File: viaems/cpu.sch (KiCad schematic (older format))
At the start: 33 parts, among them J15 Conn_01x04, J16 USB_B_Micro, J17 Conn_ARM_JTAG_SWD_10, U10 MCP2562-H-SN, U11 NCP1117-3.3_TO252, U9 STM32F407VGTx, Y1 8 Mhz

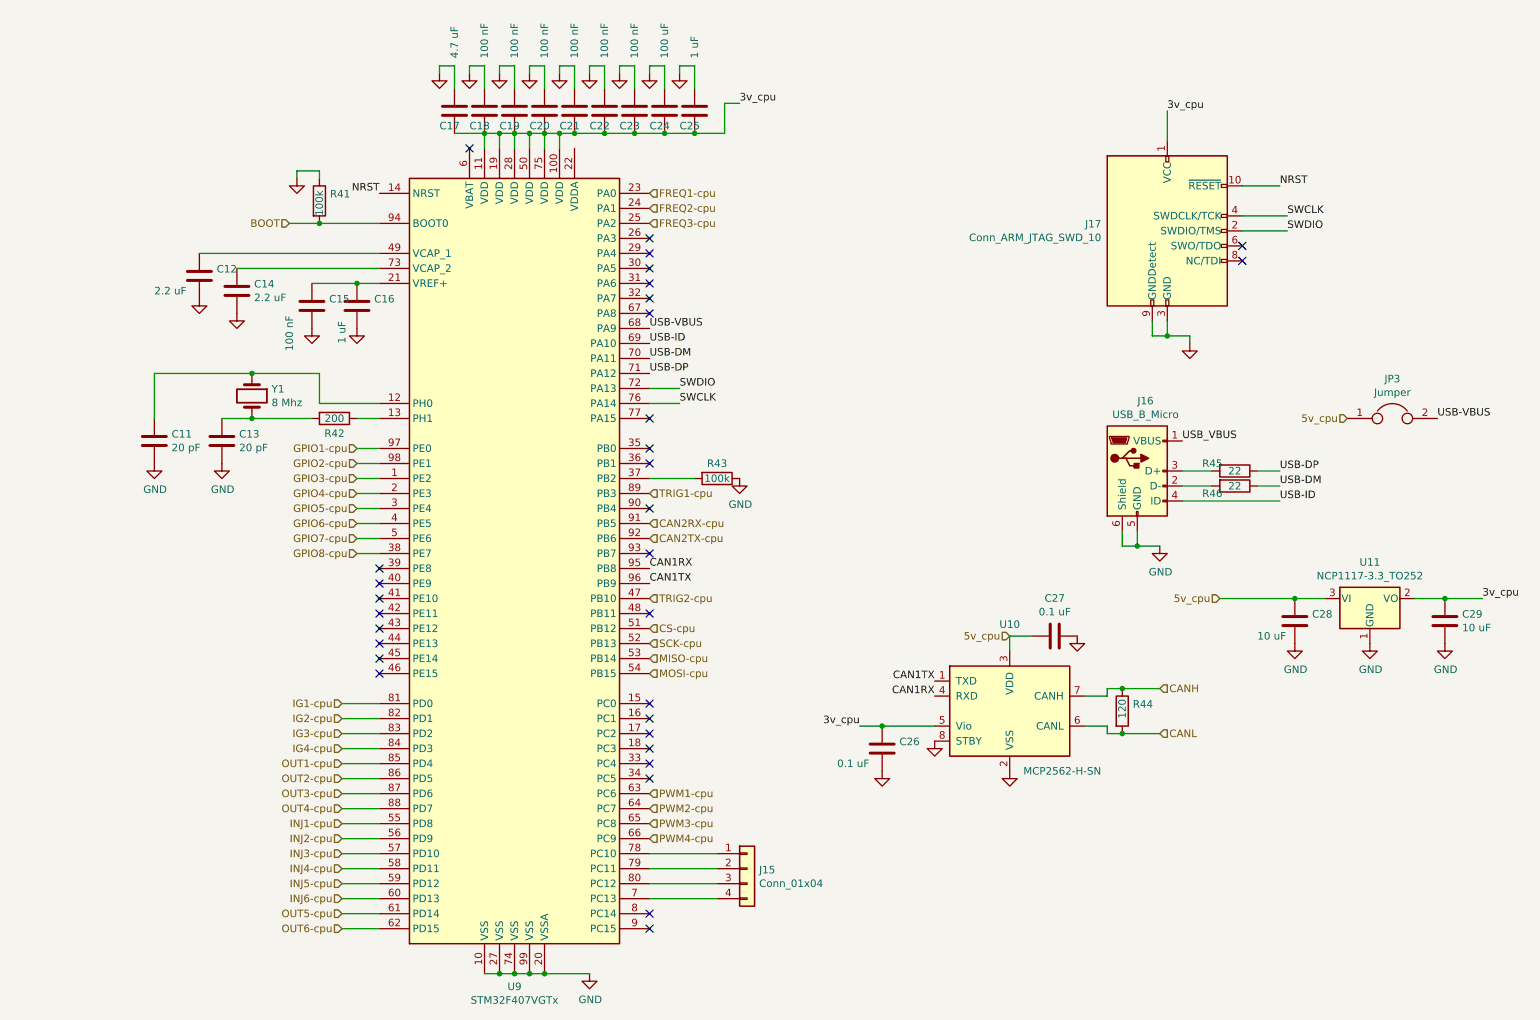
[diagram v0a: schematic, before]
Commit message: More progress. Calling schematic complete, board partially routed
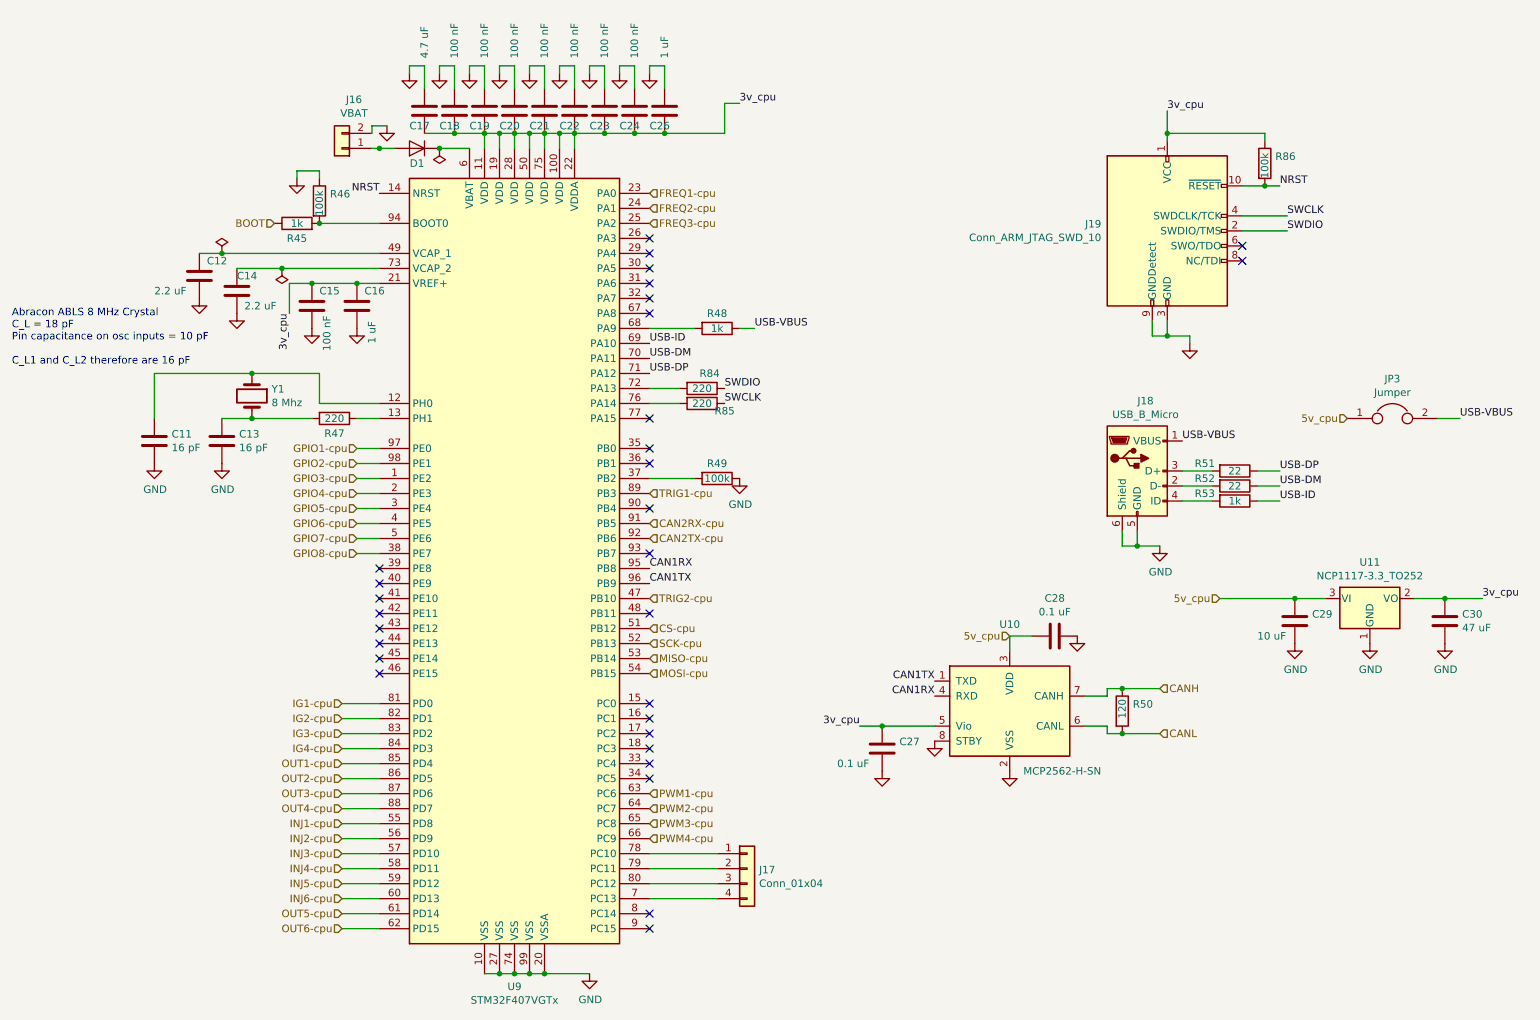
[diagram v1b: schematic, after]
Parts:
- removed C24: 100 uF, symbol Device:C
- added C18: 100 nF, Capacitor_SMD:C_0805_2012Metric_Pad1.15x1.40mm_HandSolder, symbol Device:C
- added D1: D, Diode_SMD:D_0805_2012Metric_Pad1.15x1.40mm_HandSolder, symbol Device:D
- added J16: VBAT, Connector_PinHeader_2.54mm:PinHeader_1x02_P2.54mm_Vertical, symbol Connector_Generic:Conn_01x02
- added R45, R48, R53: 1k, Resistor_SMD:R_0805_2012Metric_Pad1.15x1.40mm_HandSolder, symbol Device:R
- added R84, R85: 220, Resistor_SMD:R_0805_2012Metric_Pad1.15x1.40mm_HandSolder, symbol Device:R
- added R86: 100k, Resistor_SMD:R_0805_2012Metric_Pad1.15x1.40mm_HandSolder, symbol Device:R
- C11, C13: value 20 pF -> 16 pF; footprint (none) -> Capacitor_SMD:C_0805_2012Metric_Pad1.15x1.40mm_HandSolder
- C12, C14, C15, C16, C17: footprint (none) -> Capacitor_SMD:C_0805_2012Metric_Pad1.15x1.40mm_HandSolder
- C19: renamed from C18; footprint (none) -> Capacitor_SMD:C_0805_2012Metric_Pad1.15x1.40mm_HandSolder
- C20: renamed from C19; footprint (none) -> Capacitor_SMD:C_0805_2012Metric_Pad1.15x1.40mm_HandSolder
- C21: renamed from C20; footprint (none) -> Capacitor_SMD:C_0805_2012Metric_Pad1.15x1.40mm_HandSolder
- C22: renamed from C21; footprint (none) -> Capacitor_SMD:C_0805_2012Metric_Pad1.15x1.40mm_HandSolder
- C23: renamed from C22; footprint (none) -> Capacitor_SMD:C_0805_2012Metric_Pad1.15x1.40mm_HandSolder
- C24: renamed from C23; footprint (none) -> Capacitor_SMD:C_0805_2012Metric_Pad1.15x1.40mm_HandSolder
- C26: renamed from C25; footprint (none) -> Capacitor_SMD:C_0805_2012Metric_Pad1.15x1.40mm_HandSolder
- C27: renamed from C26; footprint (none) -> Capacitor_SMD:C_0805_2012Metric_Pad1.15x1.40mm_HandSolder
- C28: renamed from C27; footprint (none) -> Capacitor_SMD:C_0805_2012Metric_Pad1.15x1.40mm_HandSolder
- C29: renamed from C28; footprint (none) -> Capacitor_SMD:C_0805_2012Metric_Pad1.15x1.40mm_HandSolder; Digikey-Part (none) -> 587-3417-1-ND
- C30: renamed from C29; value 10 uF -> 47 uF; footprint (none) -> Capacitor_SMD:C_1206_3216Metric_Pad1.42x1.75mm_HandSolder; Digikey-Part (none) -> 478-9009-1-ND
- J17: renamed from J15; footprint (none) -> Connector_PinHeader_2.54mm:PinHeader_1x04_P2.54mm_Vertical
- J18: renamed from J16; footprint (none) -> Connector_USB:USB_Micro-B_Amphenol_10103594-0001LF_Horizontal; Digikey-Part (none) -> H125279CT-ND
- J19: renamed from J17; Digikey-Part (none) -> SAM9438-ND
- JP3: footprint (none) -> Connector_PinHeader_2.54mm:PinHeader_1x02_P2.54mm_Vertical
- R46: renamed from R41; footprint (none) -> Resistor_SMD:R_0805_2012Metric_Pad1.15x1.40mm_HandSolder
- R47: renamed from R42; value 200 -> 220; footprint (none) -> Resistor_SMD:R_0805_2012Metric_Pad1.15x1.40mm_HandSolder
- R49: renamed from R43; footprint (none) -> Resistor_SMD:R_0805_2012Metric_Pad1.15x1.40mm_HandSolder
- R50: renamed from R44; footprint (none) -> Resistor_SMD:R_0805_2012Metric_Pad1.15x1.40mm_HandSolder
- R51: renamed from R45; footprint (none) -> Resistor_SMD:R_0805_2012Metric_Pad1.15x1.40mm_HandSolder
- R52: renamed from R46; footprint (none) -> Resistor_SMD:R_0805_2012Metric_Pad1.15x1.40mm_HandSolder
- U11: Digikey-Part (none) -> NCP1117DT33T5GOSCT-ND
- Y1: footprint (none) -> Crystal:Crystal_HC49-U_Vertical; Digikey-Part (none) -> 535-10212-1-ND
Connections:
- net USB_VBUS is gone; now on net USB-VBUS: J18.1 (VBUS)
- net 3v_cpu: now also C15.1, C16.1, U9.21 (VREF+), U9.22 (VDDA), C18.2, R86.1
- net BOOT: now also R45.1; no longer R46.2, U9.94 (BOOT0)
- net GND: now also C18.1, J16.2 (Pin_2)
- net NRST: now also R86.2
- net SWCLK: now also R85.1; no longer U9.76 (PA14)
- net SWDIO: now also R84.1; no longer U9.72 (PA13)
- net USB-ID: now also R53.1; no longer J18.4 (ID)
- net USB-VBUS: now also R48.1; no longer U9.68 (PA9)
- net at U9.6 (VBAT): now also D1.1 (K)
- new net: R45.2, R46.2, U9.94 (BOOT0)
- new net: R48.2, U9.68 (PA9)
- new net: R84.2, U9.72 (PA13)
- new net: R85.2, U9.76 (PA14)
- new net: J18.4 (ID), R53.2
- new net: D1.2 (A), J16.1 (Pin_1)
- no-connect marks 31 -> 30
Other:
- note added: "Abracon ABLS 8 MHz Crystal\nC_L = 18 pF\nPin capacitance on osc inputs = 10 pF\n\nC_L1 and C_L2 therefore are 16 pF"
- moved on the sheet: C17, C26

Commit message: More routing
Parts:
- C15, C18, C19, C20, C21, C22, C23, C24: value 100 nF -> 0.1 uF
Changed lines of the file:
@@
 P 3850 1200
 F 0 "C19" H 3750 1100 50  0000 L CNN
-F 1 "100 nF" V 3850 1550 50  0000 L CNN
+F 1 "0.1 uF" V 3850 1550 50  0000 L CNN
 F 2 "Capacitor_SMD:C_0805_2012Metric_Pad1.15x1.40mm_HandSolder" H 3888 1050 50  0001 C CNN
 F 3 "~" H 3850 1200 50  0001 C CNN
@@
 P 4050 1200
 F 0 "C20" H 3950 1100 50  0000 L CNN
-F 1 "100 nF" V 4050 1550 50  0000 L CNN
+F 1 "0.1 uF" V 4050 1550 50  0000 L CNN
 F 2 "Capacitor_SMD:C_0805_2012Metric_Pad1.15x1.40mm_HandSolder" H 4088 1050 50  0001 C CNN
 F 3 "~" H 4050 1200 50  0001 C CNN
@@
 P 4250 1200
 F 0 "C21" H 4150 1100 50  0000 L CNN
-F 1 "100 nF" V 4250 1550 50  0000 L CNN
+F 1 "0.1 uF" V 4250 1550 50  0000 L CNN
 F 2 "Capacitor_SMD:C_0805_2012Metric_Pad1.15x1.40mm_HandSolder" H 4288 1050 50  0001 C CNN
 F 3 "~" H 4250 1200 50  0001 C CNN
@@
 P 4450 1200
 F 0 "C22" H 4350 1100 50  0000 L CNN
-F 1 "100 nF" V 4450 1550 50  0000 L CNN
+F 1 "0.1 uF" V 4450 1550 50  0000 L CNN
 F 2 "Capacitor_SMD:C_0805_2012Metric_Pad1.15x1.40mm_HandSolder" H 4488 1050 50  0001 C CNN
 F 3 "~" H 4450 1200 50  0001 C CNN
@@
 P 4650 1200
 F 0 "C23" H 4550 1100 50  0000 L CNN
-F 1 "100 nF" V 4650 1550 50  0000 L CNN
+F 1 "0.1 uF" V 4650 1550 50  0000 L CNN
 F 2 "Capacitor_SMD:C_0805_2012Metric_Pad1.15x1.40mm_HandSolder" H 4688 1050 50  0001 C CNN
 F 3 "~" H 4650 1200 50  0001 C CNN
@@
 P 4850 1200
 F 0 "C24" H 4750 1100 50  0000 L CNN
-F 1 "100 nF" V 4850 1550 50  0000 L CNN
+F 1 "0.1 uF" V 4850 1550 50  0000 L CNN
 F 2 "Capacitor_SMD:C_0805_2012Metric_Pad1.15x1.40mm_HandSolder" H 4888 1050 50  0001 C CNN
 F 3 "~" H 4850 1200 50  0001 C CNN
@@
 P 2700 2500
 F 0 "C15" H 2750 2600 50  0000 L CNN
-F 1 "100 nF" V 2800 2200 50  0000 L CNN
+F 1 "0.1 uF" V 2800 2200 50  0000 L CNN
 F 2 "Capacitor_SMD:C_0805_2012Metric_Pad1.15x1.40mm_HandSolder" H 2738 2350 50  0001 C CNN
 F 3 "~" H 2700 2500 50  0001 C CNN
@@
 	3750 1450 3550 1450
 Wire Wire Line
-	3250 1450 3150 1450
-Wire Wire Line
 	3100 1300 3200 1300
 $Comp
@@
 P 3650 1200
 F 0 "C18" H 3550 1100 50  0000 L CNN
-F 1 "100 nF" V 3650 1550 50  0000 L CNN
+F 1 "0.1 uF" V 3650 1550 50  0000 L CNN
 F 2 "Capacitor_SMD:C_0805_2012Metric_Pad1.15x1.40mm_HandSolder" H 3688 1050 50  0001 C CNN
 F 3 "~" H 3650 1200 50  0001 C CNN
@@
 	-1   0    0    1
 $EndComp
-Connection ~ 3150 1450
-Wire Wire Line
-	3150 1450 3100 1450
 Connection ~ 3550 1450
+Wire Wire Line
+	3100 1450 3250 1450
 $EndSCHEMATC

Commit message: Finished routing
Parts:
- added JP1: Jumper, Connector_PinHeader_2.54mm:PinHeader_1x02_P2.54mm_Vertical, symbol Device:Jumper
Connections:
- net 3v_cpu: now also JP1.1
- net BOOT: no longer names the net of R45.1
- net BOOT: now also JP1.2
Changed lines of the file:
@@
 Wire Wire Line
 	2600 1600 2600 1650
-Text HLabel 2450 1950 0    50   Input ~ 0
-BOOT
 Text HLabel 2900 5150 0    50   Input ~ 0
 IG1-cpu
@@
 Wire Wire Line
 	3100 1450 3250 1450
+$Comp
+L Device:Jumper JP1
+U 1 1 5C1828E1
+P 2150 1950
+F 0 "JP1" H 2150 2214 50  0000 C CNN
+F 1 "Jumper" H 2150 2123 50  0000 C CNN
+F 2 "Connector_PinHeader_2.54mm:PinHeader_1x02_P2.54mm_Vertical" H 2150 1950 50  0001 C CNN
+F 3 "~" H 2150 1950 50  0001 C CNN
+	1    2150 1950
+	1    0    0    -1
+$EndComp
+Text Label 1850 1950 2    50   ~ 0
+3v_cpu
+Entry Bus Bus
+	1950 1400 2050 1500
 $EndSCHEMATC

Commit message: Misc fixes
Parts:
- C11, C13: Digikey-Part (none) -> 311-4228-1-ND
- C12: Digikey-Part (none) -> 1276-1188-1-ND; Notes ESR <2.2 ohm -> ESR < 2.2 ohm
- C14: Digikey-Part (none) -> 1276-1188-1-ND
- C15, C18, C19, C20, C21, C22, C23, C24, C27, C28: Digikey-Part (none) -> 478-10836-1-ND
- C16, C26: Digikey-Part (none) -> 1276-1066-1-ND
- C17: Digikey-Part (none) -> 445-14527-1-ND
- D1: Digikey-Part (none) -> 478-7802-1-ND
- J16, JP1, JP3: Digikey-Part (none) -> 952-2262-ND
- J17: Digikey-Part (none) -> 732-5317-ND
- J18: Digikey-Part H125279CT-ND -> 609-4050-1-ND
- R45, R48, R53: Digikey-Part (none) -> RNCP0805FTD1K00CT-ND
- R46, R49, R86: Digikey-Part (none) -> P100KDACT-ND
- R47, R84, R85: Digikey-Part (none) -> A129741CT-ND
- R50: Digikey-Part (none) -> P16874CT-ND
- R51, R52: Digikey-Part (none) -> A130124CT-ND
- U10: Digikey-Part (none) -> MCP2562-H/SN
- U9: Digikey-Part (none) -> 497-17438-ND
